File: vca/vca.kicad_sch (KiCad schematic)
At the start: 27 parts, among them J1 Conn_01x02_Socket, J2 Conn_01x02_Socket, J3 Conn_01x02_Socket, J5 Conn_01x03_Socket, Q1 BC548C, Q2 BC548C, U1 TL074

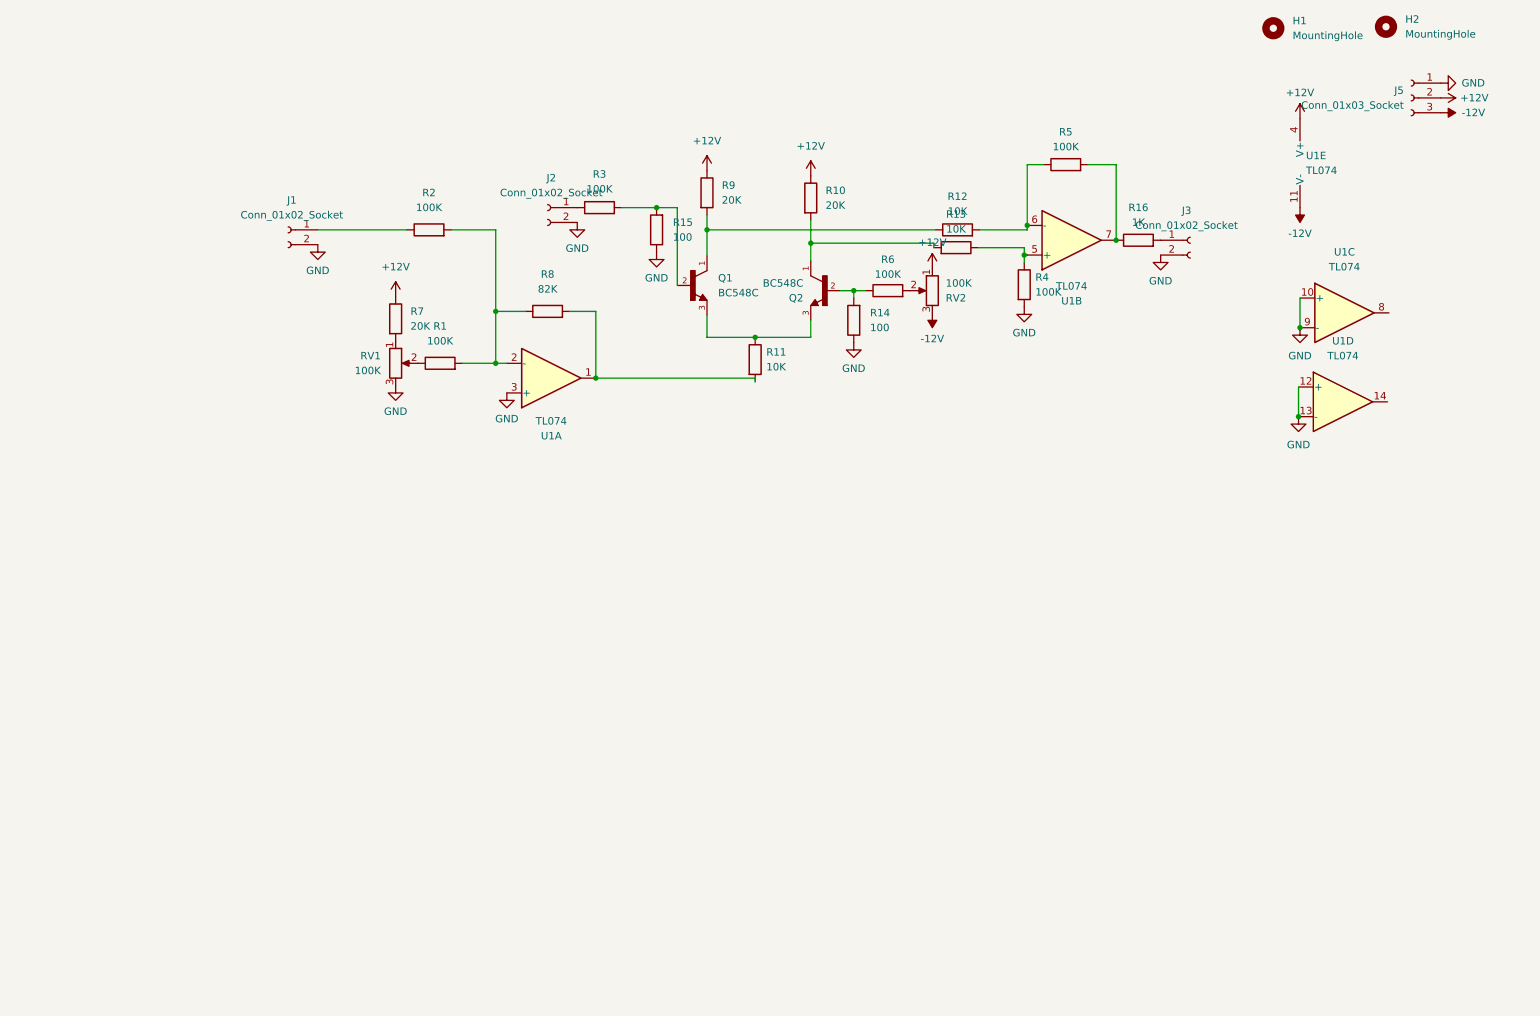
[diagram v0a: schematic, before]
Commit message: add the eg and reroute the vca.
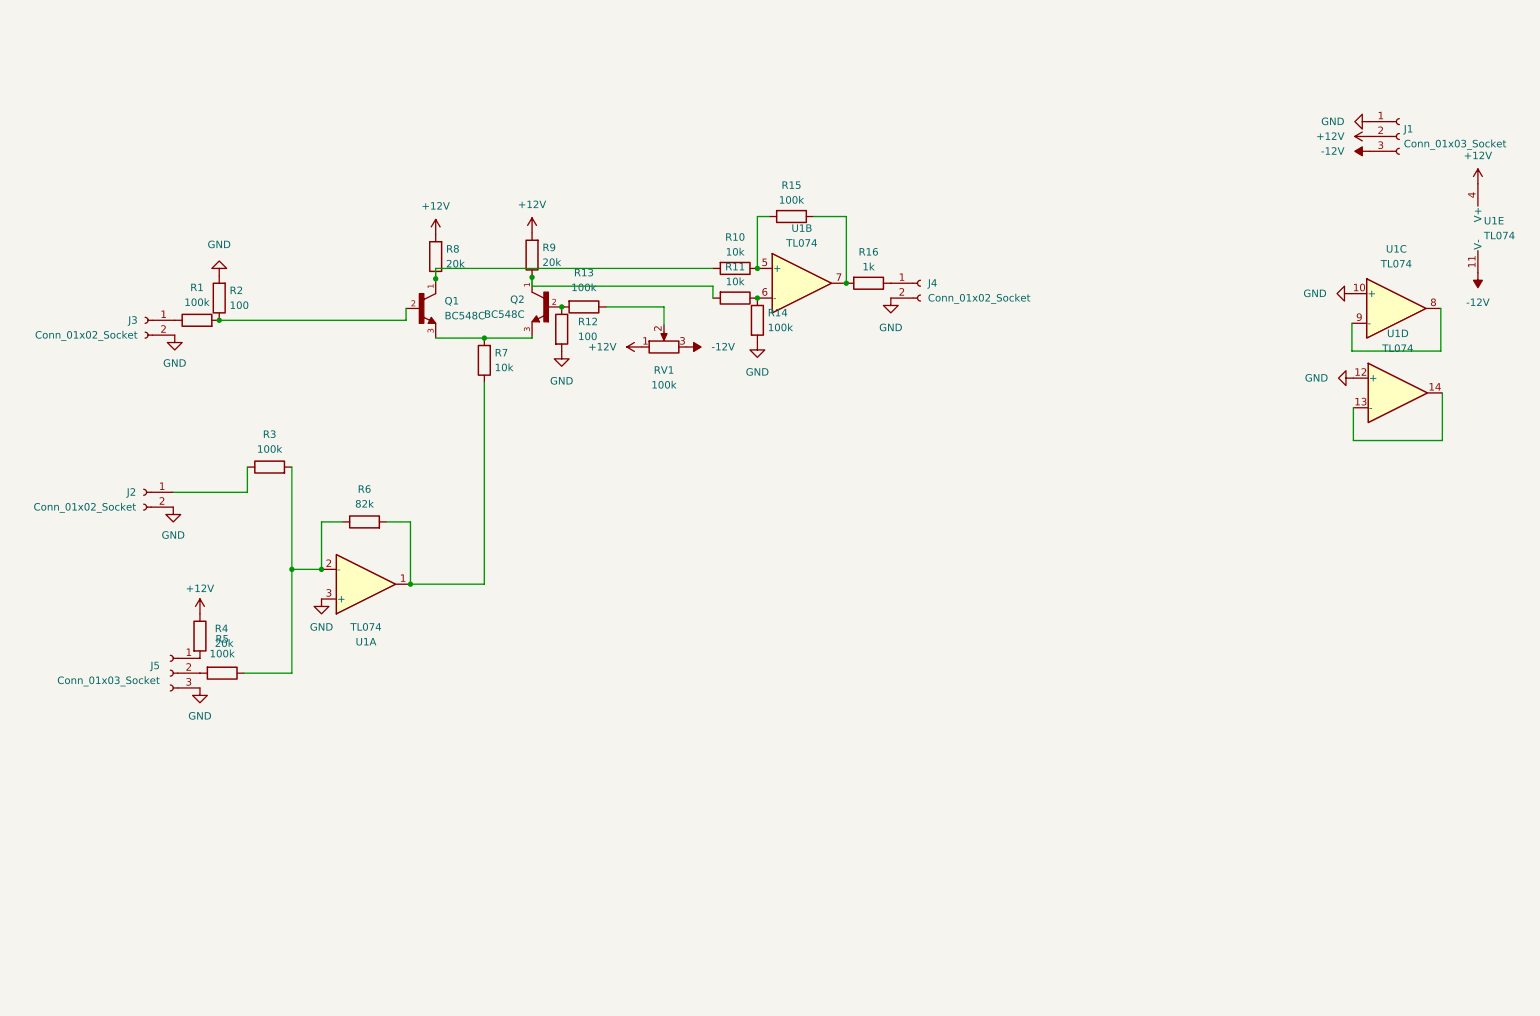
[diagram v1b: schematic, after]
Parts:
- removed H1, H2: MountingHole, MountingHole:MountingHole_2.5mm, symbol Mechanical:MountingHole
- removed J1: Conn_01x02_Socket, Connector_PinHeader_2.54mm:PinHeader_1x02_P2.54mm_Vertical, symbol Connector:Conn_01x02_Socket
- removed RV2: 100K, Connector_PinHeader_2.54mm:PinHeader_1x03_P2.54mm_Vertical, symbol Device:R_Potentiometer
- added J1: Conn_01x03_Socket, my_library:my_really_cool_3pin, symbol Connector:Conn_01x03_Socket
- added J4: Conn_01x02_Socket, my_library:my_really_cool_2pin, symbol Connector:Conn_01x02_Socket
- J2, J3: footprint Connector_PinHeader_2.54mm:PinHeader_1x02_P2.54mm_Vertical -> my_library:my_really_cool_2pin
- J5: footprint Connector_PinHeader_2.54mm:PinHeader_1x03_P2.54mm_Vertical -> my_library:my_really_cool_3pin
- R1, R3, R5: value 100K -> 100k
- R10, R7: value 20K -> 10k
- R11: value 10K -> 10k
- R12: value 10K -> 100
- R13: value 10K -> 100k
- R14, R15: value 100 -> 100k
- R16: value 1K -> 1k
- R2: value 100K -> 100
- R4: value 100K -> 20k
- R6: value 100K -> 82k
- R8: value 82K -> 20k
- R9: value 20K -> 20k
- RV1: value 100K -> 100k; footprint Connector_PinHeader_2.54mm:PinHeader_1x03_P2.54mm_Vertical -> Potentiometer_THT:Potentiometer_Vishay_T73XW_Horizontal
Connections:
- net +12V: now also R4.1, R8.2, R9.2, RV1.1, J1.2 (Pin_2); no longer J5.2 (Pin_2), R10.1, R7.1, R9.1
- net -12V: now also RV1.3, J1.3 (Pin_3); no longer J5.3 (Pin_3)
- net GND: now also J5.3 (Pin_3), R12.2, R14.2, R2.2, J1.1 (Pin_1), J4.2 (Pin_2); no longer J5.1 (Pin_1), R14.1, R15.1, R4.2, RV1.3, U1.13 (-), U1.9 (-)
- net at Q1.3, Q2.3: now also R7.2; no longer R11.1
- net at U1.8: now also U1.9 (-)
- net at R6.2: now also R7.1, U1.1
- net at R2.1: now also Q1.2, R1.2
- net at J3.1 (Pin_1): now also R1.1; no longer R16.2
- net at RV1.2: now also R13.1; no longer R1.1
- net at U1.14: now also U1.13 (-)
- new net: R3.2, R5.1, R6.1, U1.2 (-)
- new net: J5.2 (Pin_2), R5.2
- new net: R11.1, R14.1, U1.6 (-)
- new net: Q2.2, R12.1, R13.2
- new net: Q2.1, R11.2, R9.1
- new net: Q1.1, R10.2, R8.1
- new net: J4.1 (Pin_1), R16.1
- new net: R15.1, R16.2, U1.7
- new net: J5.1 (Pin_1), R4.2
- new net: R10.1, R15.2, U1.5 (+)

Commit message: turn vca to dual vca add mounting holes
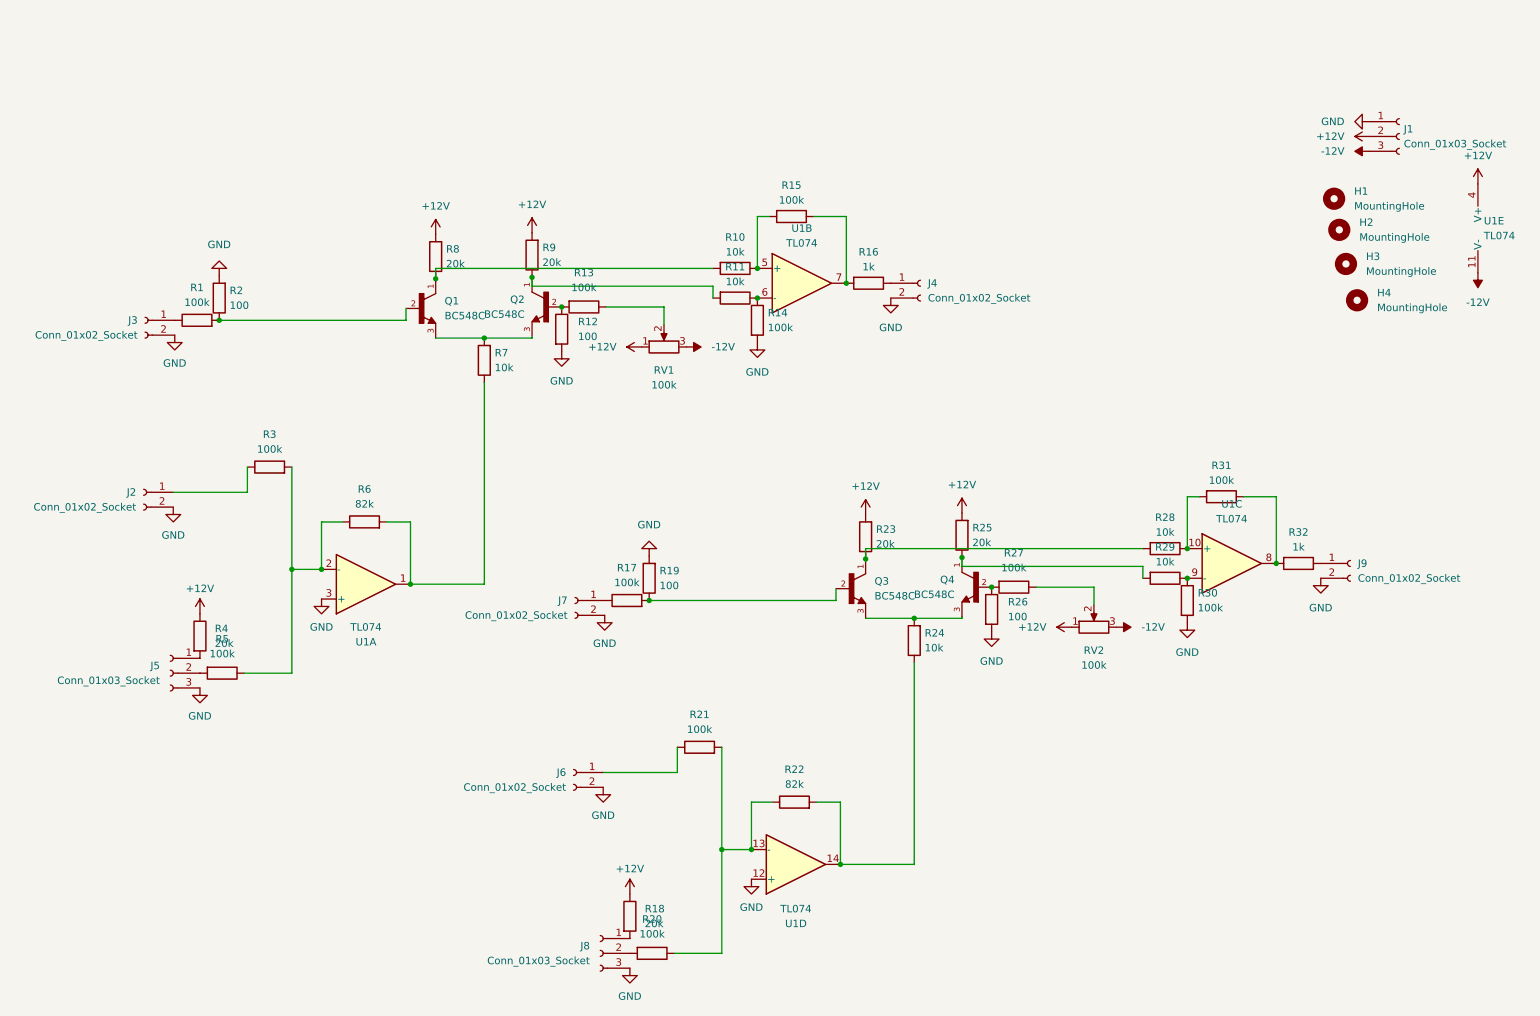
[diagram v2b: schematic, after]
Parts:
- added H1, H2, H3, H4: MountingHole, MountingHole:MountingHole_2.1mm, symbol Mechanical:MountingHole
- added J6, J7, J9: Conn_01x02_Socket, my_library:my_really_cool_2pin, symbol Connector:Conn_01x02_Socket
- added J8: Conn_01x03_Socket, my_library:my_really_cool_3pin, symbol Connector:Conn_01x03_Socket
- added Q3, Q4: BC548C, BC548C:TO92250P510H770-3, symbol BC548C:BC548C
- added R17, R20, R21, R27, R30, R31: 100k, Resistor_THT:R_Axial_DIN0204_L3.6mm_D1.6mm_P7.62mm_Horizontal, symbol Device:R
- added R18, R23, R25: 20k, Resistor_THT:R_Axial_DIN0204_L3.6mm_D1.6mm_P7.62mm_Horizontal, symbol Device:R
- added R19, R26: 100, Resistor_THT:R_Axial_DIN0204_L3.6mm_D1.6mm_P7.62mm_Horizontal, symbol Device:R
- added R22: 82k, Resistor_THT:R_Axial_DIN0204_L3.6mm_D1.6mm_P7.62mm_Horizontal, symbol Device:R
- added R24, R28, R29: 10k, Resistor_THT:R_Axial_DIN0204_L3.6mm_D1.6mm_P7.62mm_Horizontal, symbol Device:R
- added R32: 1k, Resistor_THT:R_Axial_DIN0204_L3.6mm_D1.6mm_P7.62mm_Horizontal, symbol Device:R
- added RV2: 100k, Potentiometer_THT:Potentiometer_Vishay_T73XW_Horizontal, symbol Device:R_Potentiometer
- U1: footprint Package_DIP:DIP-14_W7.62mm -> my_library:my_dip14
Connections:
- net +12V: now also R18.1, R23.2, R25.2, RV2.1
- net -12V: now also RV2.3
- net GND: now also J6.2 (Pin_2), J7.2 (Pin_2), J8.3 (Pin_3), J9.2 (Pin_2), R19.2, R26.2, R30.2; no longer U1.10 (+)
- net at U1.8: now also R31.1, R32.2; no longer U1.9 (-)
- net at U1.13 (-): now also R20.1, R21.2, R22.1; no longer U1.14
- new net: R28.1, R31.2, U1.10 (+)
- new net: Q3.1, R23.1, R28.2
- new net: R22.2, R24.1, U1.14
- new net: J8.2 (Pin_2), R20.2
- new net: J9.1 (Pin_1), R32.1
- new net: R29.1, R30.1, U1.9 (-)
- new net: Q4.1, R25.1, R29.2
- new net: Q4.2, R26.1, R27.2
- new net: Q3.3, Q4.3, R24.2
- new net: Q3.2, R17.2, R19.1
- new net: R27.1, RV2.2
- new net: J7.1 (Pin_1), R17.1
- new net: J8.1 (Pin_1), R18.2
- new net: J6.1 (Pin_1), R21.1
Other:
- moved on the sheet: U1C, U1D
